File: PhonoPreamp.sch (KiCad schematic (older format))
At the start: 101 parts, among them J1 Conn_01x03, J2 Conn_01x02, J3 Conn_01x02, J4 Conn_01x02, J5 Conn_01x02, J6 Conn_01x01, J7 Conn_01x01, J8 Conn_01x01, J9 Conn_01x01, Q1 2N5551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

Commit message: Bigger capacitor footprints
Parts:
- C1, C2: footprint Capacitors_THT:CP_Radial_D10.0mm_P5.00mm -> Capacitors_THT:CP_Radial_D14.0mm_P5.00mm
- C4, C5: footprint Capacitors_THT:CP_Radial_D7.5mm_P2.50mm -> Capacitors_THT:CP_Radial_D14.0mm_P5.00mm
- U3, U4: footprint Housings_DIP:DIP-8_W7.62mm -> Housings_DIP:DIP-8_W7.62mm_Socket
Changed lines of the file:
@@
 F 0 "C1" H 1775 6500 50  0000 L CNN
 F 1 "3300 uF" H 1775 6300 50  0000 L CNN
-F 2 "Capacitors_THT:CP_Radial_D10.0mm_P5.00mm" H 1788 6250 50  0001 C CNN
+F 2 "Capacitors_THT:CP_Radial_D14.0mm_P5.00mm" H 1788 6250 50  0001 C CNN
 F 3 "" H 1750 6400 50  0001 C CNN
 	1    1750 6400
@@
 F 0 "C2" H 1775 6850 50  0000 L CNN
 F 1 "3300 uF" H 1775 6650 50  0000 L CNN
-F 2 "Capacitors_THT:CP_Radial_D10.0mm_P5.00mm" H 1788 6600 50  0001 C CNN
+F 2 "Capacitors_THT:CP_Radial_D14.0mm_P5.00mm" H 1788 6600 50  0001 C CNN
 F 3 "" H 1750 6750 50  0001 C CNN
 	1    1750 6750
@@
 F 0 "C4" H 2825 6450 50  0000 L CNN
 F 1 "47 uF" H 2825 6250 50  0000 L CNN
-F 2 "Capacitors_THT:CP_Radial_D7.5mm_P2.50mm" H 2838 6200 50  0001 C CNN
+F 2 "Capacitors_THT:CP_Radial_D14.0mm_P5.00mm" H 2838 6200 50  0001 C CNN
 F 3 "" H 2800 6350 50  0001 C CNN
 	1    2800 6350
@@
 F 0 "C5" H 2825 6850 50  0000 L CNN
 F 1 "47 uF" H 2825 6650 50  0000 L CNN
-F 2 "Capacitors_THT:CP_Radial_D7.5mm_P2.50mm" H 2838 6600 50  0001 C CNN
+F 2 "Capacitors_THT:CP_Radial_D14.0mm_P5.00mm" H 2838 6600 50  0001 C CNN
 F 3 "" H 2800 6750 50  0001 C CNN
 	1    2800 6750
@@
 $EndComp
 $Comp
-L GND #PWR1
+L GND #PWR01
 U 1 1 5F9CBF02
 P 1000 6850
-F 0 "#PWR1" H 1000 6600 50  0001 C CNN
+F 0 "#PWR01" H 1000 6600 50  0001 C CNN
 F 1 "GND" H 1000 6700 50  0000 C CNN
 F 2 "" H 1000 6850 50  0001 C CNN
@@
 $EndComp
 $Comp
-L +15V #PWR4
+L +15V #PWR02
 U 1 1 5F9CBF72
 P 2800 5800
-F 0 "#PWR4" H 2800 5650 50  0001 C CNN
+F 0 "#PWR02" H 2800 5650 50  0001 C CNN
 F 1 "+15V" H 2800 5940 50  0000 C CNN
 F 2 "" H 2800 5800 50  0001 C CNN
@@
 $EndComp
 $Comp
-L GND #PWR8
+L GND #PWR03
 U 1 1 5F9CD483
 P 3150 7250
-F 0 "#PWR8" H 3150 7000 50  0001 C CNN
+F 0 "#PWR03" H 3150 7000 50  0001 C CNN
 F 1 "GND" H 3150 7100 50  0000 C CNN
 F 2 "" H 3150 7250 50  0001 C CNN
@@
 $EndComp
 $Comp
-L GND #PWR2
+L GND #PWR04
 U 1 1 5F9D02E7
 P 1700 2000
-F 0 "#PWR2" H 1700 1750 50  0001 C CNN
+F 0 "#PWR04" H 1700 1750 50  0001 C CNN
 F 1 "GND" H 1700 1850 50  0000 C CNN
 F 2 "" H 1700 2000 50  0001 C CNN
@@
 F 0 "U3" H 3400 1700 50  0000 L CNN
 F 1 "LM4562" H 3600 1700 50  0000 L CNN
-F 2 "Housings_DIP:DIP-8_W7.62mm" H 3400 1500 50  0001 C CNN
+F 2 "Housings_DIP:DIP-8_W7.62mm_Socket" H 3400 1500 50  0001 C CNN
 F 3 "" H 3400 1500 50  0001 C CNN
 	2    3400 1500
@@
 $EndComp
 $Comp
-L +15V #PWR9
+L +15V #PWR05
 U 1 1 5F9D20C2
 P 3300 800
-F 0 "#PWR9" H 3300 650 50  0001 C CNN
+F 0 "#PWR05" H 3300 650 50  0001 C CNN
 F 1 "+15V" H 3300 940 50  0000 C CNN
 F 2 "" H 3300 800 50  0001 C CNN
@@
 $EndComp
 $Comp
-L GND #PWR6
+L GND #PWR06
 U 1 1 5F9D301C
 P 2850 1200
-F 0 "#PWR6" H 2850 950 50  0001 C CNN
+F 0 "#PWR06" H 2850 950 50  0001 C CNN
 F 1 "GND" H 2850 1050 50  0000 C CNN
 F 2 "" H 2850 1200 50  0001 C CNN
@@
 $EndComp
 $Comp
-L GND #PWR13
+L GND #PWR07
 U 1 1 5F9D771A
 P 3700 2500
-F 0 "#PWR13" H 3700 2250 50  0001 C CNN
+F 0 "#PWR07" H 3700 2250 50  0001 C CNN
 F 1 "GND" H 3700 2350 50  0000 C CNN
 F 2 "" H 3700 2500 50  0001 C CNN
@@
 F 0 "U3" H 5650 1800 50  0000 L CNN
 F 1 "LM4562" H 5850 1800 50  0000 L CNN
-F 2 "Housings_DIP:DIP-8_W7.62mm" H 5650 1600 50  0001 C CNN
+F 2 "Housings_DIP:DIP-8_W7.62mm_Socket" H 5650 1600 50  0001 C CNN
 F 3 "" H 5650 1600 50  0001 C CNN
 	1    5650 1600
@@
 $EndComp
 $Comp
-L GND #PWR3
+L GND #PWR08
 U 1 1 5F9DCE3B
 P 1700 4200
-F 0 "#PWR3" H 1700 3950 50  0001 C CNN
+F 0 "#PWR08" H 1700 3950 50  0001 C CNN
 F 1 "GND" H 1700 4050 50  0000 C CNN
 F 2 "" H 1700 4200 50  0001 C CNN
@@
 F 0 "U4" H 3400 3900 50  0000 L CNN
 F 1 "LM4562" H 3600 3900 50  0000 L CNN
-F 2 "Housings_DIP:DIP-8_W7.62mm" H 3400 3700 50  0001 C CNN
+F 2 "Housings_DIP:DIP-8_W7.62mm_Socket" H 3400 3700 50  0001 C CNN
 F 3 "" H 3400 3700 50  0001 C CNN
 	2    3400 3700
@@
 $EndComp
 $Comp
-L +15V #PWR11
+L +15V #PWR09
 U 1 1 5F9DCE60
 P 3300 3000
-F 0 "#PWR11" H 3300 2850 50  0001 C CNN
+F 0 "#PWR09" H 3300 2850 50  0001 C CNN
 F 1 "+15V" H 3300 3140 50  0000 C CNN
 F 2 "" H 3300 3000 50  0001 C CNN
@@
 $EndComp
 $Comp
-L GND #PWR7
+L GND #PWR010
 U 1 1 5F9DCE78
 P 2850 3400
-F 0 "#PWR7" H 2850 3150 50  0001 C CNN
+F 0 "#PWR010" H 2850 3150 50  0001 C CNN
 F 1 "GND" H 2850 3250 50  0000 C CNN
 F 2 "" H 2850 3400 50  0001 C CNN
@@
 $EndComp
 $Comp
-L GND #PWR14
+L GND #PWR011
 U 1 1 5F9DCF1E
 P 3700 4700
-F 0 "#PWR14" H 3700 4450 50  0001 C CNN
+F 0 "#PWR011" H 3700 4450 50  0001 C CNN
 F 1 "GND" H 3700 4550 50  0000 C CNN
 F 2 "" H 3700 4700 50  0001 C CNN
@@
 F 0 "U4" H 5650 4050 50  0000 L CNN
 F 1 "LM4562" H 5850 4050 50  0000 L CNN
-F 2 "Housings_DIP:DIP-8_W7.62mm" H 5650 3800 50  0001 C CNN
+F 2 "Housings_DIP:DIP-8_W7.62mm_Socket" H 5650 3800 50  0001 C CNN
 F 3 "" H 5650 3800 50  0001 C CNN
 	1    5650 3800

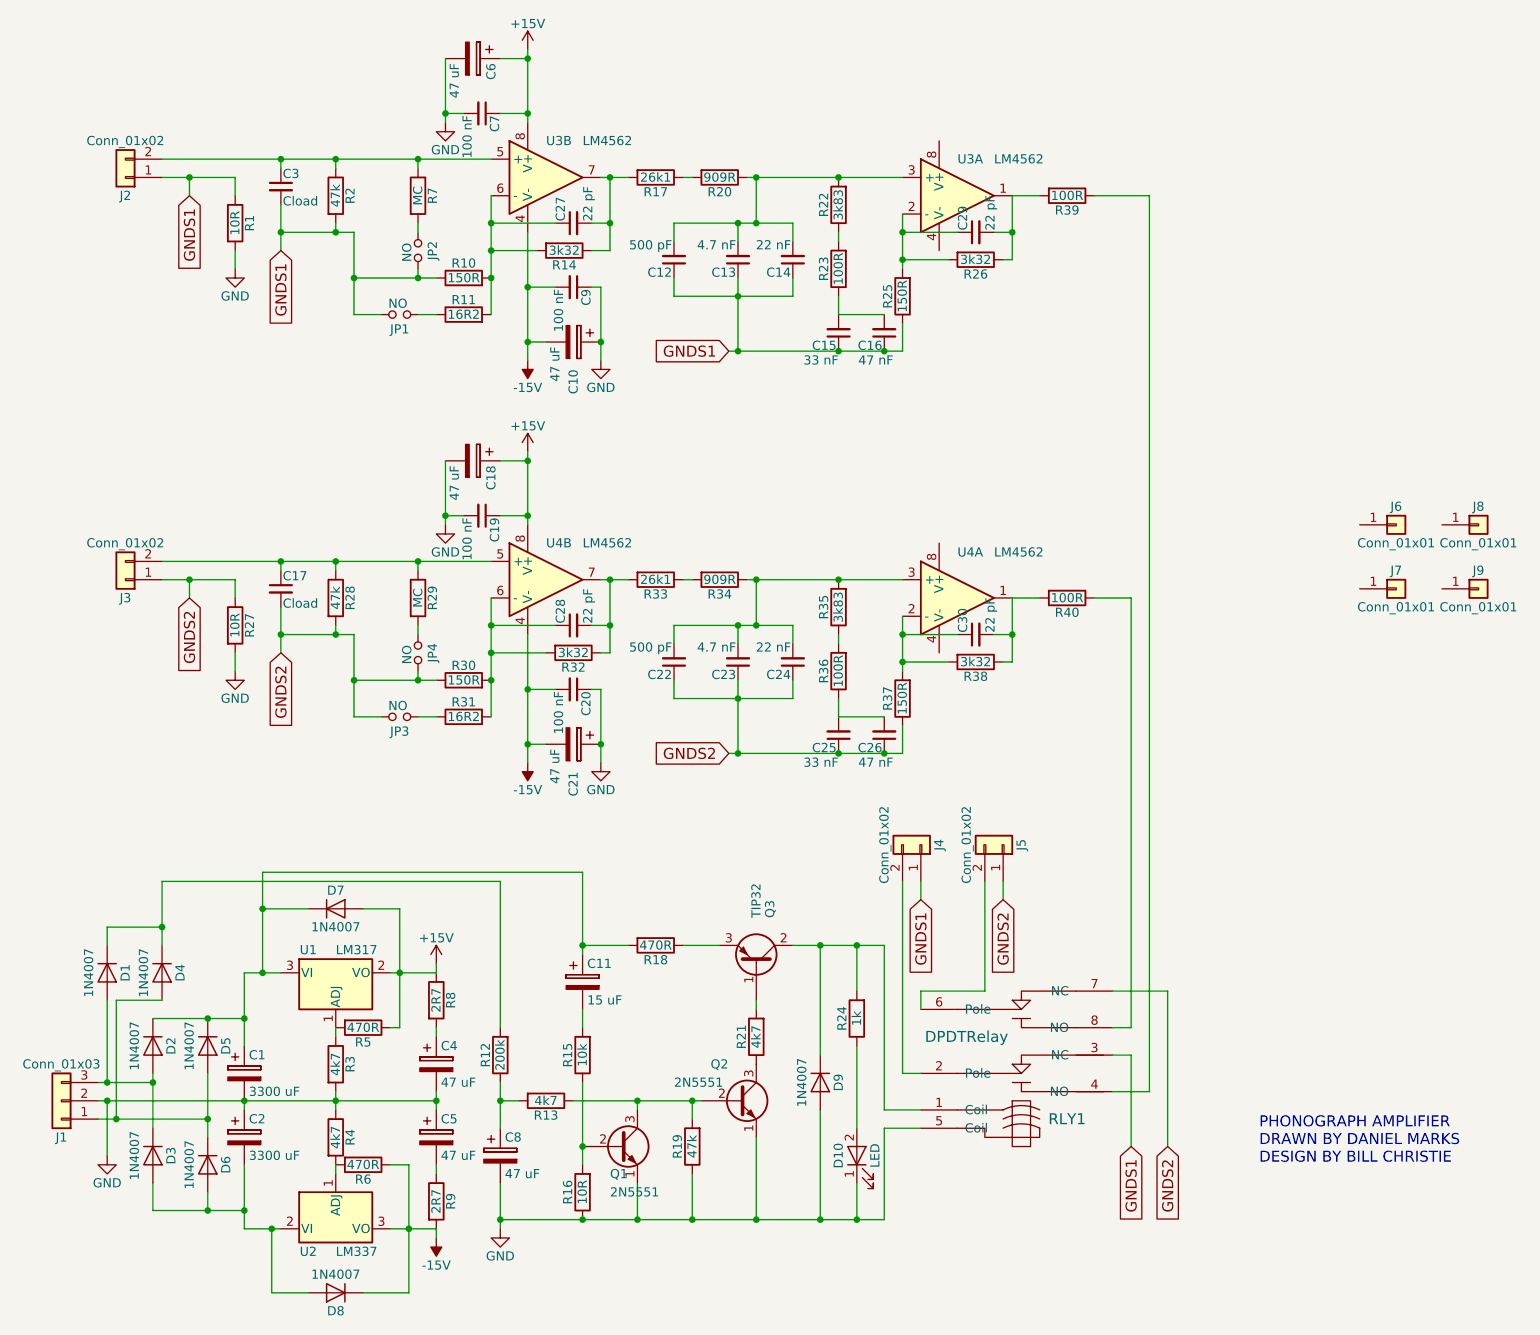
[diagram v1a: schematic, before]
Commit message: Added rumble filter
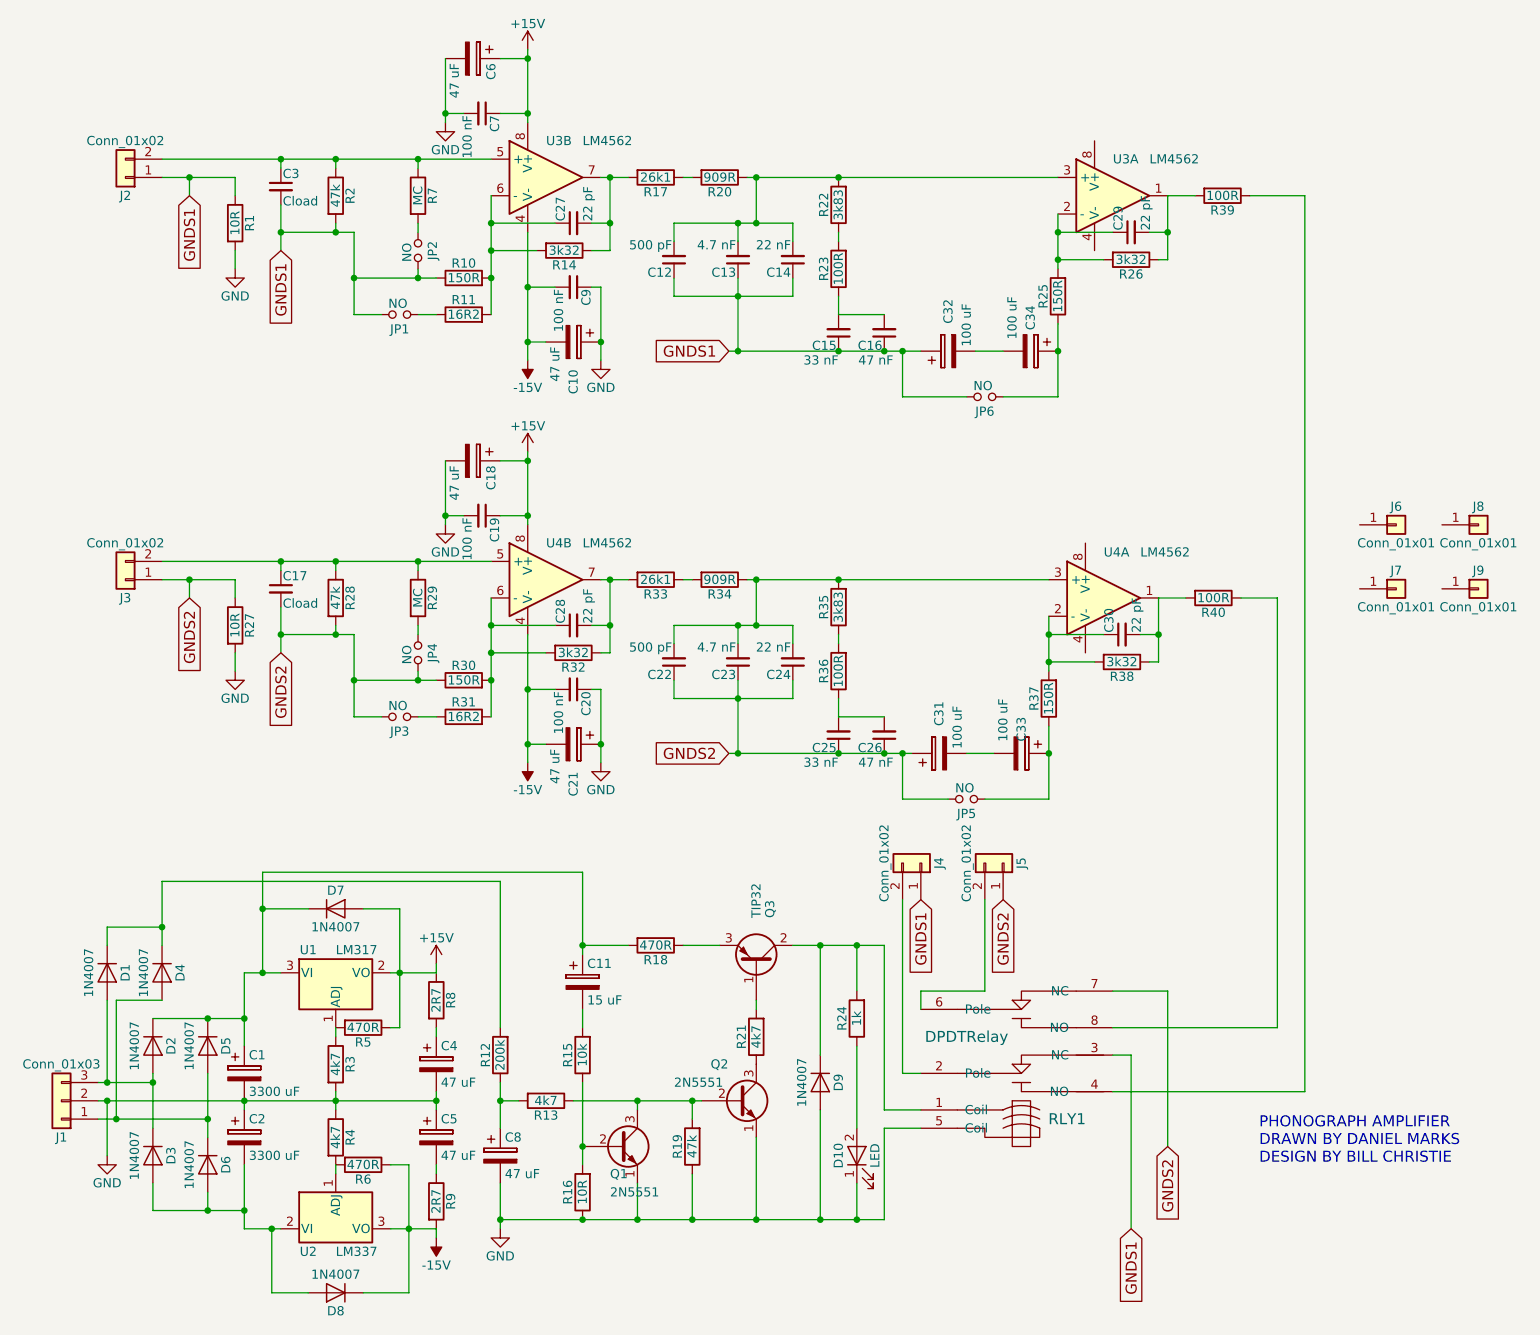
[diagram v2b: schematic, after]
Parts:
- added C31, C32, C33, C34: 100 uF, Capacitors_THT:CP_Radial_D7.5mm_P2.50mm, symbol CP
- added JP5, JP6: NO, Pin_Headers:Pin_Header_Straight_1x02_Pitch2.54mm, symbol Jumper_NO_Small
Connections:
- net GNDS1: now also C32.1, JP6.2; no longer R25.1
- net GNDS2: now also C31.1, JP5.2; no longer R37.1
- new net: C34.1, JP6.1, R25.1
- new net: C33.1, JP5.1, R37.1
- new net: C32.2, C34.2
- new net: C31.2, C33.2
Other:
- moved on the sheet: C29, C30, J4, J5, R25, R26, R37, R38, R39, R40, U3A, U4A
